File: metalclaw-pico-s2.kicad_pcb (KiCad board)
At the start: 2 copper layers, 3 parts, among them J1 USB_C_Receptacle_USB2.0_14P, U1 ESP32-S2

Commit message: Initial schematic connections
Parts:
- removed A1: RaspberryPi_Pico, Module:RaspberryPi_Pico_Common_Unspecified
- added A2: RaspberryPi_Pico, Module:RaspberryPi_Pico_SMD_HandSolder, F.Cu at (163.8, 98.9)
- added U2: W25Q16JVSS, Package_SO:SOIC-8_5.3x5.3mm_P1.27mm, F.Cu at (164.0, 107.0)
- added U3: APS6404L-3SQRx-SN, Package_SO:SOIC-8_3.9x4.9mm_P1.27mm, F.Cu at (164.0, 115.5)
- moved J1 53.4 mm to (163.4, 73.6), turned to 0 degrees
- moved U1 53.1 mm to (164.0, 96.6), turned to -45 degrees
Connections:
- J1 pad A1: Net-(J1-GND-PadA1) -> GND
- J1 pad A12: Net-(J1-GND-PadA1) -> GND
- J1 pad A6: unconnected-(J1-D+-PadA6) -> Net-(U1-GPIO20/USB_D+)
- J1 pad A7: unconnected-(J1-D--PadA7) -> Net-(U1-GPIO19/USB_D-)
- J1 pad B1: Net-(J1-GND-PadA1) -> GND
- J1 pad B12: Net-(J1-GND-PadA1) -> GND
- J1 pad B6: unconnected-(J1-D+-PadB6) -> /GP28
- J1 pad B7: unconnected-(J1-D--PadB7) -> Net-(U1-GPIO19/USB_D-)
- U1 pad 10: unconnected-(U1-GPIO5-Pad10) -> /GP5
- U1 pad 11: unconnected-(U1-GPIO6-Pad11) -> /GP6
- U1 pad 12: unconnected-(U1-GPIO7-Pad12) -> /GP7
- U1 pad 13: unconnected-(U1-GPIO8-Pad13) -> /GP8
- U1 pad 14: unconnected-(U1-GPIO9-Pad14) -> /GP9
- U1 pad 15: unconnected-(U1-GPIO10-Pad15) -> /GP10
- U1 pad 16: unconnected-(U1-GPIO11-Pad16) -> /GP11
- U1 pad 17: unconnected-(U1-GPIO12-Pad17) -> /GP12
- U1 pad 18: unconnected-(U1-GPIO13-Pad18) -> /GP13
- U1 pad 19: unconnected-(U1-GPIO14-Pad19) -> /GP14
- U1 pad 21: unconnected-(U1-XTAL_32K_P-Pad21) -> /RUN
- U1 pad 22: unconnected-(U1-XTAL_32K_N-Pad22) -> /3V3_EN
- U1 pad 23: unconnected-(U1-DAC_1-Pad23) -> /GP26
- U1 pad 24: unconnected-(U1-DAC_2-Pad24) -> /GP27
- U1 pad 25: unconnected-(U1-GPIO19/USB_D--Pad25) -> Net-(U1-GPIO19/USB_D-)
- U1 pad 26: unconnected-(U1-GPIO20/USB_D+-Pad26) -> Net-(U1-GPIO20/USB_D+)
- U1 pad 28: unconnected-(U1-GPIO21-Pad28) -> Net-(U1-GPIO21)
- U1 pad 29: unconnected-(U1-SPICS1-Pad29) -> Net-(U1-SPICS1)
- U1 pad 31: unconnected-(U1-SPIHD-Pad31) -> Net-(U1-SPIHD)
- U1 pad 32: unconnected-(U1-SPIWP-Pad32) -> Net-(U1-SPIWP)
- U1 pad 33: unconnected-(U1-SPICS0-Pad33) -> Net-(U1-SPICS0)
- U1 pad 34: unconnected-(U1-SPICLK-Pad34) -> Net-(U1-SPICLK)
- U1 pad 35: unconnected-(U1-SPIQ-Pad35) -> Net-(U1-SPIQ)
- U1 pad 36: unconnected-(U1-SPID-Pad36) -> Net-(U1-SPID)
- U1 pad 37: unconnected-(U1-GPIO33-Pad37) -> /GP15
- U1 pad 38: unconnected-(U1-GPIO34-Pad38) -> /GP16
- U1 pad 39: unconnected-(U1-GPIO35-Pad39) -> /GP17
- U1 pad 40: unconnected-(U1-GPIO36-Pad40) -> /GP18
- U1 pad 41: unconnected-(U1-GPIO37-Pad41) -> /GP20
- U1 pad 42: unconnected-(U1-GPIO38-Pad42) -> /GP19
- U1 pad 43: unconnected-(U1-MTCK-Pad43) -> /MTCK
- U1 pad 44: unconnected-(U1-MTD0-Pad44) -> /MTDO
- U1 pad 46: unconnected-(U1-MDTI-Pad46) -> /MTDI
- U1 pad 47: unconnected-(U1-MTMS-Pad47) -> /MTMS
- U1 pad 48: unconnected-(U1-U0TXD-Pad48) -> /SWCLK
- U1 pad 49: unconnected-(U1-U0RXD-Pad49) -> /SWDIO
- U1 pad 5: unconnected-(U1-GPIO0-Pad5) -> /GP0
- U1 pad 50: unconnected-(U1-GPIO45-Pad50) -> /GP21
- U1 pad 55: unconnected-(U1-GPIO46-Pad55) -> /GP22
- U1 pad 57: unconnected-(U1-GND-Pad57) -> GND
- U1 pad 6: unconnected-(U1-GPIO1-Pad6) -> /GP1
- U1 pad 7: unconnected-(U1-GPIO2-Pad7) -> /GP2
- U1 pad 8: unconnected-(U1-GPIO3-Pad8) -> /GP3
- U1 pad 9: unconnected-(U1-GPIO4-Pad9) -> /GP4

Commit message: Specify series resistor resistance and footprint
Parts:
- added R1: 5.1k, Capacitor_SMD:C_0402_1005Metric, F.Cu at (182.5, 67.8)
- added R10: 220, Capacitor_SMD:C_0402_1005Metric, F.Cu at (185.8, 67.8)
- added R11: 220, Capacitor_SMD:C_0402_1005Metric, F.Cu at (185.8, 69.8)
- added R12: 220, Capacitor_SMD:C_0402_1005Metric, F.Cu at (185.8, 71.8)
- added R13: 220, Capacitor_SMD:C_0402_1005Metric, F.Cu at (185.8, 73.8)
- added R14: 220, Capacitor_SMD:C_0402_1005Metric, F.Cu at (185.8, 75.8)
- added R15: 220, Capacitor_SMD:C_0402_1005Metric, F.Cu at (185.8, 77.7)
- added R16: 220, Capacitor_SMD:C_0402_1005Metric, F.Cu at (185.8, 79.7)
- added R18: 220, Capacitor_SMD:C_0402_1005Metric, F.Cu at (185.8, 81.7)
- added R19: 220, Capacitor_SMD:C_0402_1005Metric, F.Cu at (185.8, 83.7)
- added R2: 220, Capacitor_SMD:C_0402_1005Metric, F.Cu at (182.5, 69.8)
- added R20: 220, Capacitor_SMD:C_0402_1005Metric, F.Cu at (189.0, 67.8)
- added R21: 220, Capacitor_SMD:C_0402_1005Metric, F.Cu at (189.0, 69.8)
- added R22: 220, Capacitor_SMD:C_0402_1005Metric, F.Cu at (189.0, 71.8)
- added R23: 220, Capacitor_SMD:C_0402_1005Metric, F.Cu at (189.0, 73.8)
- added R24: 220, Capacitor_SMD:C_0402_1005Metric, F.Cu at (189.0, 75.8)
- added R25: 220, Capacitor_SMD:C_0402_1005Metric, F.Cu at (189.0, 77.7)
- added R26: 220, Capacitor_SMD:C_0402_1005Metric, F.Cu at (189.0, 79.7)
- added R27: 220, Capacitor_SMD:C_0402_1005Metric, F.Cu at (189.0, 81.7)
- added R28: 220, Capacitor_SMD:C_0402_1005Metric, F.Cu at (189.0, 83.7)
- added R29: 5.1k, Capacitor_SMD:C_0402_1005Metric, F.Cu at (192.3, 67.8)
- added R3: 220, Capacitor_SMD:C_0402_1005Metric, F.Cu at (182.5, 71.8)
- added R30: 5.1k, Capacitor_SMD:C_0402_1005Metric, F.Cu at (192.3, 69.8)
- added R31: 5.1k, Capacitor_SMD:C_0402_1005Metric, F.Cu at (192.3, 71.8)
- added R32: 5.1k, Capacitor_SMD:C_0402_1005Metric, F.Cu at (192.3, 73.8)
- added R33: 5.1k, Capacitor_SMD:C_0402_1005Metric, F.Cu at (192.3, 75.8)
- added R34: 5.1k, Capacitor_SMD:C_0402_1005Metric, F.Cu at (192.3, 77.7)
- added R35: 5.1k, Capacitor_SMD:C_0402_1005Metric, F.Cu at (192.3, 79.7)
- added R4: 220, Capacitor_SMD:C_0402_1005Metric, F.Cu at (182.5, 73.8)
- added R5: 220, Capacitor_SMD:C_0402_1005Metric, F.Cu at (182.5, 75.8)
- added R6: 220, Capacitor_SMD:C_0402_1005Metric, F.Cu at (182.5, 77.7)
- added R7: 220, Capacitor_SMD:C_0402_1005Metric, F.Cu at (182.5, 79.7)
- added R8: 220, Capacitor_SMD:C_0402_1005Metric, F.Cu at (157.0, 97.5)
- added R9: 220, Capacitor_SMD:C_0402_1005Metric, F.Cu at (157.5, 82.5)
- added U4: AMS1117-3.3, Package_TO_SOT_SMD:SOT-223-3_TabPin2, F.Cu at (163.5, 86.0)
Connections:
- A2 pad 33: unconnected-(A2-AGND-Pad33) -> GND
- A2 pad 34: Net-(A2-GPIO28_ADC2) -> /GP28
- A2 pad 35: unconnected-(A2-ADC_VREF-Pad35) -> +3V3
- A2 pad 36: unconnected-(A2-3V3-Pad36) -> +3V3
- J1 pad A4: Net-(J1-VBUS-PadA4) -> VBUS
- J1 pad A5: unconnected-(J1-CC1-PadA5) -> Net-(J1-CC1)
- J1 pad A9: Net-(J1-VBUS-PadA4) -> VBUS
- J1 pad B4: Net-(J1-VBUS-PadA4) -> VBUS
- J1 pad B5: unconnected-(J1-CC2-PadB5) -> Net-(J1-CC2)
- J1 pad B9: Net-(J1-VBUS-PadA4) -> VBUS
- U1 pad 10: /GP5 -> /GP4
- U1 pad 11: /GP6 -> /GP5
- U1 pad 12: /GP7 -> /GP6
- U1 pad 13: /GP8 -> /GP7
- U1 pad 14: /GP9 -> /GP8
- U1 pad 15: /GP10 -> /GP9
- U1 pad 16: /GP11 -> /GP10
- U1 pad 17: /GP12 -> /GP11
- U1 pad 18: /GP13 -> /GP12
- U1 pad 19: /GP14 -> /GP13
- U1 pad 21: /RUN -> /GP14
- U1 pad 22: /3V3_EN -> /GP15
- U1 pad 37: /GP15 -> /GP16
- U1 pad 38: /GP16 -> /GP17
- U1 pad 39: /GP17 -> /GP18
- U1 pad 40: /GP18 -> /GP19
- U1 pad 41: /GP20 -> /GP21
- U1 pad 42: /GP19 -> /GP20
- U1 pad 5: /GP0 -> /3V3_EN
- U1 pad 50: /GP21 -> /RUN
- U1 pad 6: /GP1 -> /GP0
- U1 pad 7: /GP2 -> /GP1
- U1 pad 8: /GP3 -> /GP2
- U1 pad 9: /GP4 -> /GP3

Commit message: Add crystal
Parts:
- removed U4: AMS1117-3.3, Package_TO_SOT_SMD:SOT-223-3_TabPin2
- added U5: XC6220B331MR, Package_TO_SOT_SMD:SOT-23-5, F.Cu at (165.9, 85.5)
- added Y1: XRCGB40M000F1S2FR0, Crystal:Crystal_SMD_2016-4Pin_2.0x1.6mm, F.Cu at (168.0, 91.0)
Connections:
- U1 pad 1: Net-(U1-VDDA-Pad1) -> +3V3
- U1 pad 20: unconnected-(U1-VDD3P3_RTC-Pad20) -> +3V3
- U1 pad 27: unconnected-(U1-VDD3P3_RTC_IO-Pad27) -> +3V3
- U1 pad 3: Net-(U1-VDD3P3-Pad3) -> +3V3
- U1 pad 30: unconnected-(U1-VDD_SPI-Pad30) -> +3V3
- U1 pad 4: Net-(U1-VDD3P3-Pad3) -> +3V3
- U1 pad 45: unconnected-(U1-VDD3P3_CPU-Pad45) -> +3V3
- U1 pad 51: Net-(U1-VDDA-Pad1) -> +3V3
- U1 pad 52: unconnected-(U1-XTAL_N-Pad52) -> Net-(U1-XTAL_N)
- U1 pad 53: unconnected-(U1-XTAL_P-Pad53) -> Net-(U1-XTAL_P)
- U1 pad 54: Net-(U1-VDDA-Pad1) -> +3V3

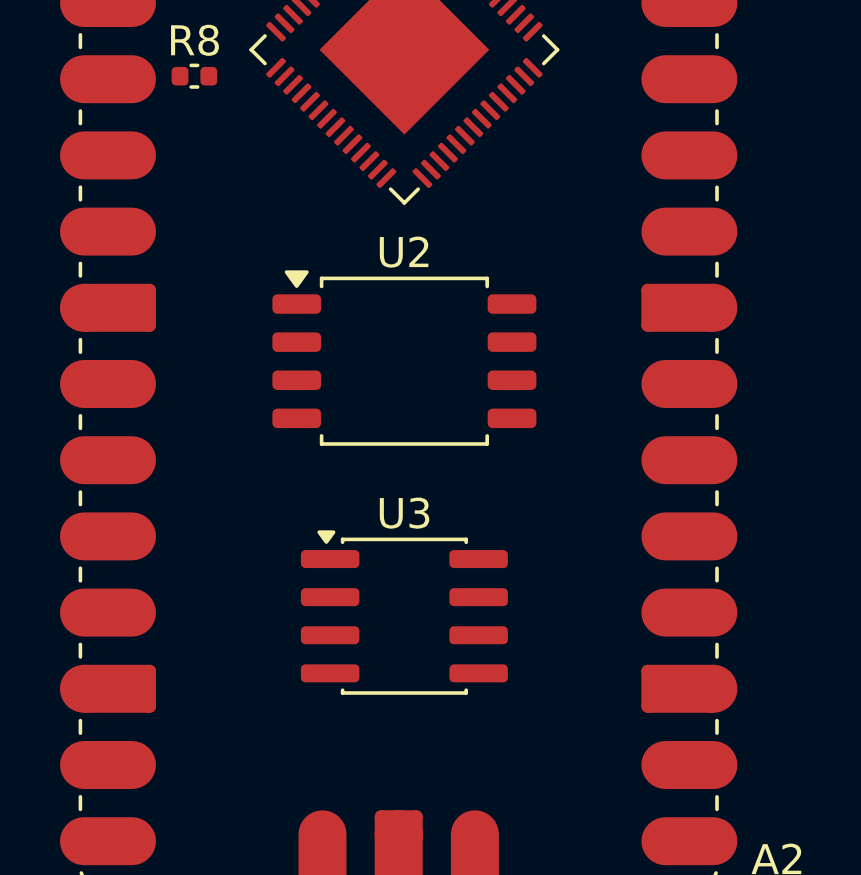
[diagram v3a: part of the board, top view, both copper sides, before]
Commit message: Specify SPI flash part and footprint
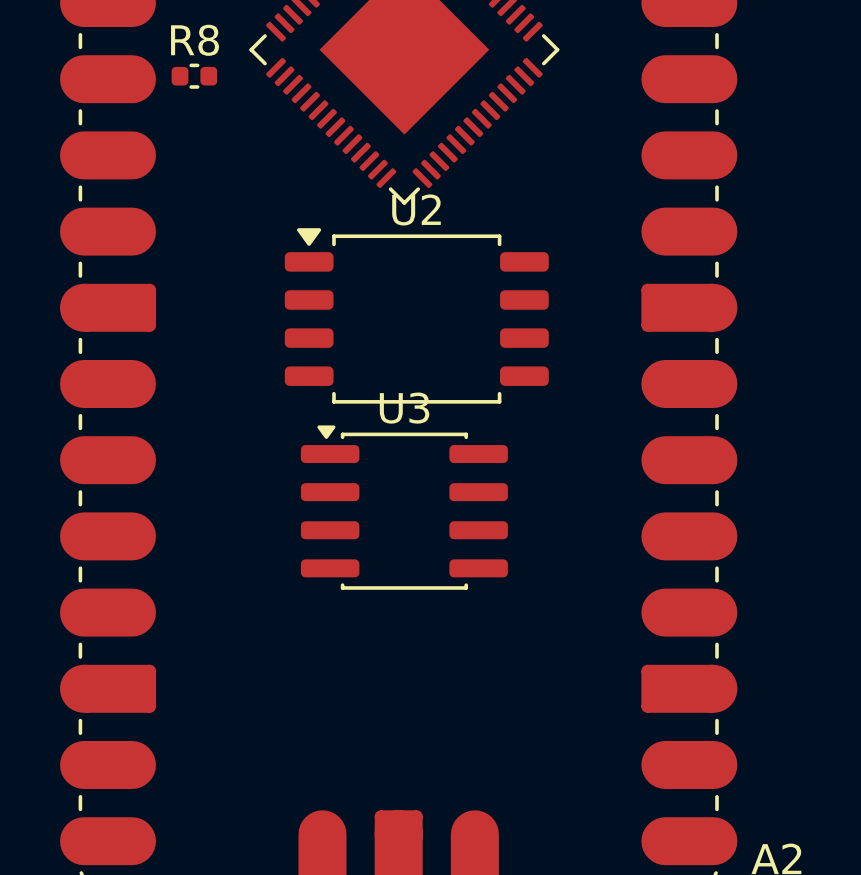
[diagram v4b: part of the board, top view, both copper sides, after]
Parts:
- U2: value W25Q16JVSS -> MX25L3236FM2I-08G-TR
- moved U3 3.50 mm to (164.0, 112.0)
- moved U2 1.46 mm to (164.4, 105.6)

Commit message: Swap SPID and SPIQ wiring to PSRAM and flash chips
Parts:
- moved U3 25.0 mm to (161.1, 87.2), turned to 180 degrees
- moved Y1 19.3 mm to (160.8, 108.9)
- moved U2 11.9 mm to (162.1, 93.9), turned to 180 degrees
- moved U1 5.93 mm to (164.1, 102.5), turned to 135 degrees
- moved U5 4.00 mm to (168.1, 82.2), turned to 90 degrees
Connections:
- U2 pad 2: Net-(U1-SPID) -> Net-(U1-SPIQ)
- U2 pad 5: Net-(U1-SPIQ) -> Net-(U1-SPID)
- U3 pad 2: Net-(U1-SPID) -> Net-(U1-SPIQ)
- U3 pad 3: Net-(U1-SPIHD) -> Net-(U1-SPIWP)
- U3 pad 5: Net-(U1-SPIQ) -> Net-(U1-SPID)
- U3 pad 7: Net-(U1-SPIWP) -> Net-(U1-SPIHD)

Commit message: Add more I2C pins
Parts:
- added J2: Conn_01x05, Connector_PinHeader_2.54mm:PinHeader_1x05_P2.54mm_Vertical, F.Cu at (158.5, 119.2)
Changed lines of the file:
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@@
+		)
+	)
+	(footprint "Connector_PinHeader_2.54mm:PinHeader_1x05_P2.54mm_Vertical"
+		(layer "F.Cu")
+		(at 158.52 119.21 90)
+		(descr "Through hole straight pin header, 1x05, 2.54mm pitch, single row")
+		(tags "Through hole pin header THT 1x05 2.54mm single row")
+		(property "Reference" "J2"
+			(at 0 -2.38 90)
+			(layer "F.SilkS")
+			(effects
+				(font
+					(size 1 1)
+					(thickness 0.15)
+				)
+			)
+		)
+		(property "Value" "Conn_01x05"
+			(at 0 12.54 90)
+			(layer "F.Fab")
+			(effects
+				(font
+					(size 1 1)
+					(thickness 0.15)
+				)
+			)
+		)
+		(property "Datasheet" "~"
+			(at 0 0 90)
+			(layer "F.Fab")
+			(hide yes)
+			(effects
+				(font
+					(size 1.27 1.27)
+					(thickness 0.15)
+				)
+			)
+		)
+		(property "Description" "Generic connector, single row, 01x05, script generated (kicad-library-utils/schlib/autogen/connector/)"
+			(at 0 0 90)
+			(layer "F.Fab")
+			(hide yes)
+			(effects
+				(font
+					(size 1.27 1.27)
+					(thickness 0.15)
+				)
+			)
+		)
+		(property ki_fp_filters "Connector*:*_1x??_*")
+		(sheetname "/")
+		(sheetfile "metalclaw-pico-s2.kicad_sch")
+		(attr through_hole)
+		(fp_line
+			(start -1.38 -1.38)
+			(end 0 -1.38)
+			(stroke
+				(width 0.12)
+				(type solid)
+			)
+			(layer "F.SilkS")
+		)
+		(fp_line
+			(start -1.38 0)
+			(end -1.38 -1.38)
+			(stroke
+				(width 0.12)
+				(type solid)
+			)
+			(layer "F.SilkS")
+		)
+		(fp_line
+			(start 1.38 1.27)
+			(end 1.38 11.54)
+			(stroke
+				(width 0.12)
+				(type solid)
+			)
+			(layer "F.SilkS")
+		)
+		(fp_line
+			(start -1.38 1.27)
+			(end 1.38 1.27)
+			(stroke
+				(width 0.12)
+				(type solid)
+			)
+			(layer "F.SilkS")
+		)
+		(fp_line
+			(start -1.38 1.27)
+			(end -1.38 11.54)
+			(stroke
+				(width 0.12)
+				(type solid)
+			)
+			(layer "F.SilkS")
+		)
+		(fp_line
+			(start -1.38 11.54)
+			(end 1.38 11.54)
+			(stroke
+				(width 0.12)
+				(type solid)
+			)
+			(layer "F.SilkS")
+		)
+		(fp_rect
+			(start -1.77 -1.77)
+			(end 1.77 11.93)
+			(stroke
+				(width 0.05)
+				(type solid)
+			)
+			(fill no)
+			(layer "F.CrtYd")
+		)
+		(fp_line
+			(start 1.27 -1.27)
+			(end 1.27 11.43)
+			(stroke
+				(width 0.1)
+				(type solid)
+			)
+			(layer "F.Fab")
+		)
+		(fp_line
+			(start -0.635 -1.27)
+			(end 1.27 -1.27)
+			(stroke
+				(width 0.1)
+				(type solid)
+			)
+			(layer "F.Fab")
+		)
+		(fp_line
+			(start -1.27 -0.635)
+			(end -0.635 -1.27)
+			(stroke
+				(width 0.1)
+				(type solid)
+			)
+			(layer "F.Fab")
+		)
+		(fp_line
+			(start 1.27 11.43)
+			(end -1.27 11.43)
+			(stroke
+				(width 0.1)
+				(type solid)
+			)
+			(layer "F.Fab")
+		)
+		(fp_line
+			(start -1.27 11.43)
+			(end -1.27 -0.635)
+			(stroke
+				(width 0.1)
+				(type solid)
+			)
+			(layer "F.Fab")
+		)
+		(fp_text user "${REFERENCE}"
+			(at 0 5.08 0)
+			(layer "F.Fab")
+			(effects
+				(font
+					(size 1 1)
+					(thickness 0.15)
+				)
+			)
+		)
+		(pad "1" thru_hole rect
+			(at 0 0 90)
+			(size 1.7 1.7)
+			(drill 1)
+			(layers "*.Cu" "*.Mask")
+			(remove_unused_layers no)
+			(net 57 "/MTCK")
+			(pinfunction "Pin_1")
+			(pintype "passive")
+		)
+		(pad "2" thru_hole circle
+			(at 0 2.54 90)
+			(size 1.7 1.7)
+			(drill 1)
+			(layers "*.Cu" "*.Mask")
+			(remove_unused_layers no)
+			(net 43 "/MTDO")
+			(pinfunction "Pin_2")
+			(pintype "passive")
+		)
+		(pad "3" thru_hole circle
+			(at 0 5.08 90)
+			(size 1.7 1.7)
+			(drill 1)
+			(layers "*.Cu" "*.Mask")
+			(remove_unused_layers no)
+			(net 78 "/MTDI")
+			(pinfunction "Pin_3")
+			(pintype "passive")
+		)
+		(pad "4" thru_hole circle
+			(at 0 7.62 90)
+			(size 1.7 1.7)
+			(drill 1)
+			(layers "*.Cu" "*.Mask")
+			(remove_unused_layers no)
+			(net 56 "/MTMS")
+			(pinfunction "Pin_4")
+			(pintype "passive")
+		)
+		(pad "5" thru_hole circle
+			(at 0 10.16 90)
+			(size 1.7 1.7)
+			(drill 1)
+			(layers "*.Cu" "*.Mask")
+			(remove_unused_layers no)
+			(net 5 "GND")
+			(pinfunction "Pin_5")
+			(pintype "passive")
+		)
+		(embedded_fonts no)
+		(model "${KICAD9_3DMODEL_DIR}/Connector_PinHeader_2.54mm.3dshapes/PinHeader_1x05_P2.54mm_Vertical.step"
+			(offset
+				(xyz 0 0 0)
+			)
+			(scale
+				(xyz 1 1 1)
+			)
+			(rotate
+				(xyz 0 0 0)
+			)
 		)
 	)

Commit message: Rearrange schematic
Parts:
- added R17: 5.1k, Capacitor_SMD:C_0402_1005Metric, F.Cu at (185.5, 90.7)
- added R36: 5.1k, Capacitor_SMD:C_0402_1005Metric, F.Cu at (185.5, 92.7)
- moved J1 23.3 mm to (179.3, 56.6)
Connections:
- R34 pad 2: /GP6 -> /GP4
- R35 pad 2: /GP7 -> /GP5

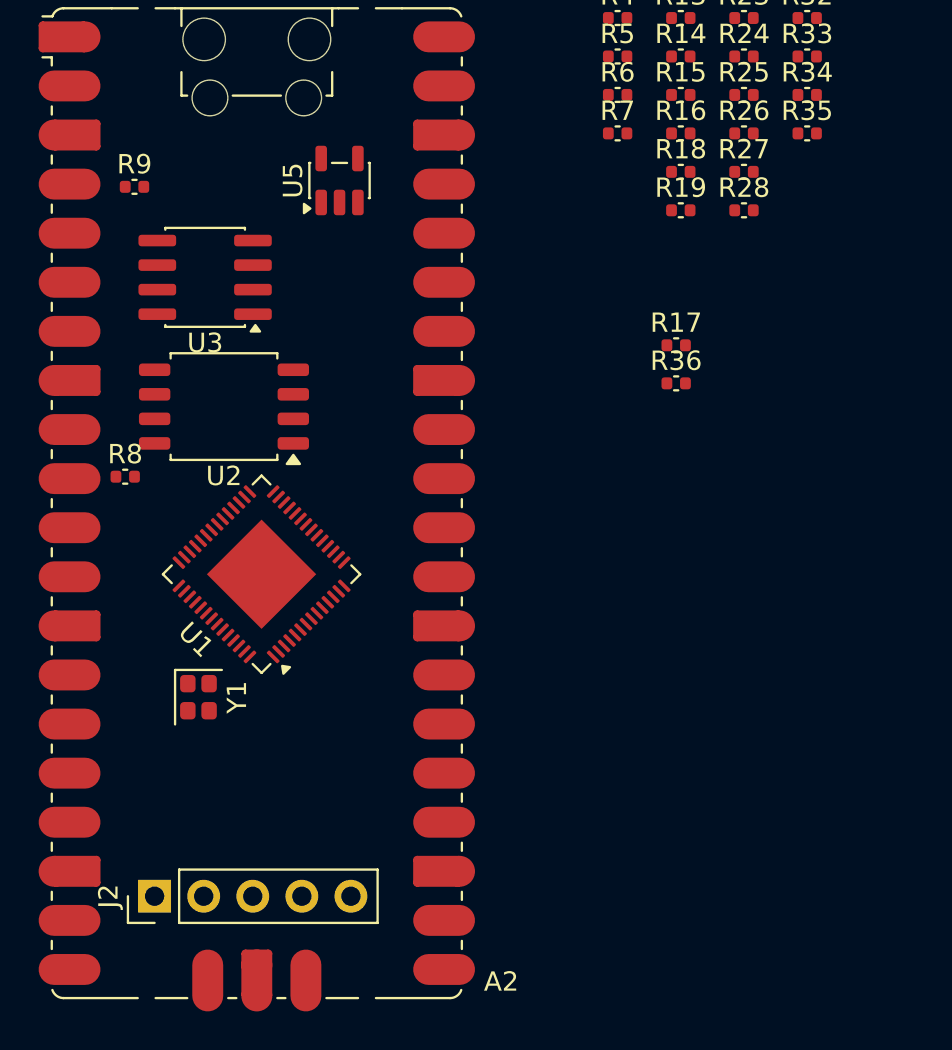
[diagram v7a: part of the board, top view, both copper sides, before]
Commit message: Add more I2C pins, JTAG connector
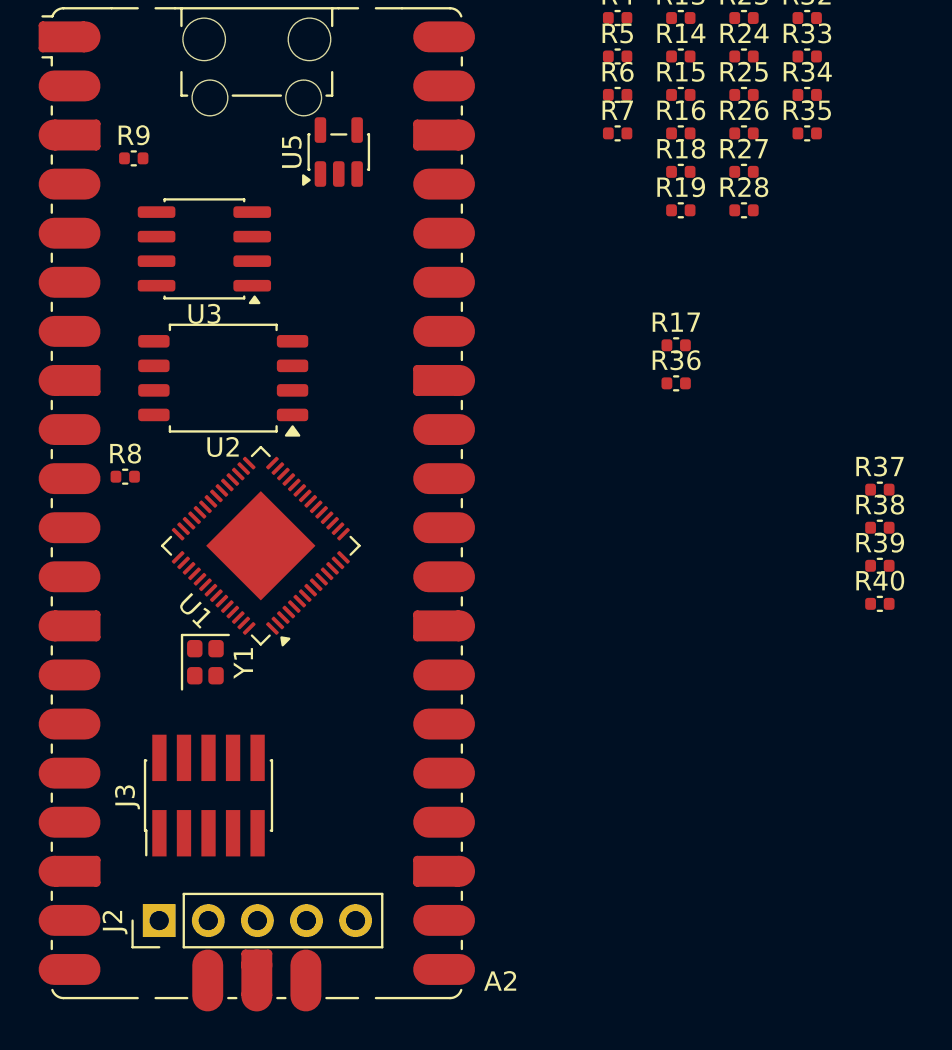
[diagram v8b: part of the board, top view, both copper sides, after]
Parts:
- added J3: Conn_02x05_Odd_Even, Connector_PinHeader_1.27mm:PinHeader_2x05_P1.27mm_Vertical_SMD, F.Cu at (161.3, 114.0)
- added R37: 5.1k, Capacitor_SMD:C_0402_1005Metric, F.Cu at (196.1, 98.2)
- added R38: 5.1k, Capacitor_SMD:C_0402_1005Metric, F.Cu at (196.1, 100.1)
- added R39: 5.1k, Capacitor_SMD:C_0402_1005Metric, F.Cu at (196.1, 102.1)
- added R40: 5.1k, Capacitor_SMD:C_0402_1005Metric, F.Cu at (196.1, 104.1)
- moved Y1 1.85 mm to (161.2, 107.1)
- moved U3 1.47 mm to (161.1, 85.7)
- moved U2 1.47 mm to (162.1, 92.4)
- moved R9 1.47 mm to (157.4, 81.0)
- moved U1 1.47 mm to (164.0, 101.1)
- moved U5 1.47 mm to (168.1, 80.7)
- moved J2 1.28 mm to (158.8, 120.5)
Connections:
- J2 pad 1: /MTCK -> /MTMS
- J2 pad 2: /MTDO -> /MTCK
- J2 pad 3: /MTDI -> /MTDO
- J2 pad 4: /MTMS -> /MTDI
